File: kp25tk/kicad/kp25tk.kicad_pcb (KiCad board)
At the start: 2 copper layers, 97.5 x 159 mm, 60 parts, among them J1 Host Connector, J2 Config Header, J3 Power In, J4 Row Select In, J5 Column Out, J6 NMI Out, J7 Reset Out, J8 Switch, SW0 KEY00, SW1 KEY01, SW10 KEY0A, SW11 KEY0B, SW12 KEY0C, SW13 KEY0D, SW14 KEY0E, SW15 KEY0F, SW16 KEY10, SW17 KEY11, SW18 KEY12, SW19 KEY13, SW2 KEY02, SW20 KEY14, SW21 KEY15, SW22 KEY16, SW23 KEY17, SW24 NMI, SW25 RESET, SW27 SWITCH, SW3 KEY03, SW4 KEY04, SW5 KEY05, SW6 KEY06, SW7 KEY07, SW8 KEY08, SW9 KEY09, U1 74LS14

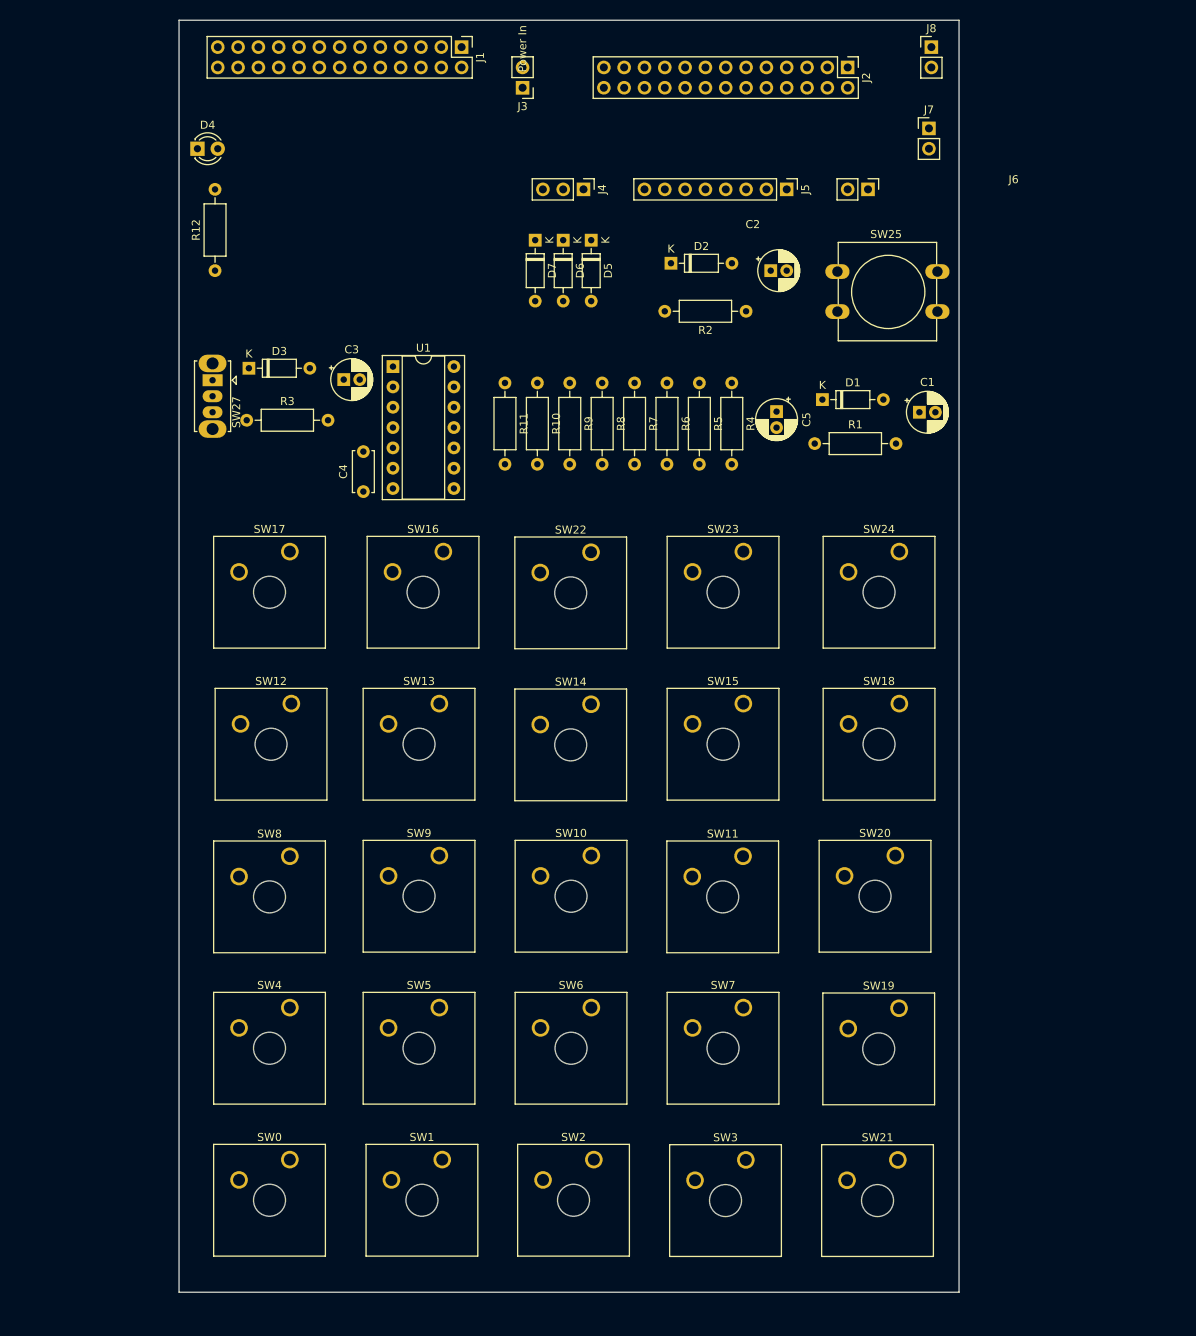
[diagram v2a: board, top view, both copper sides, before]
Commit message: kp25tk/: v0.0.4 Use resistor array and greatly compactify top of PCB
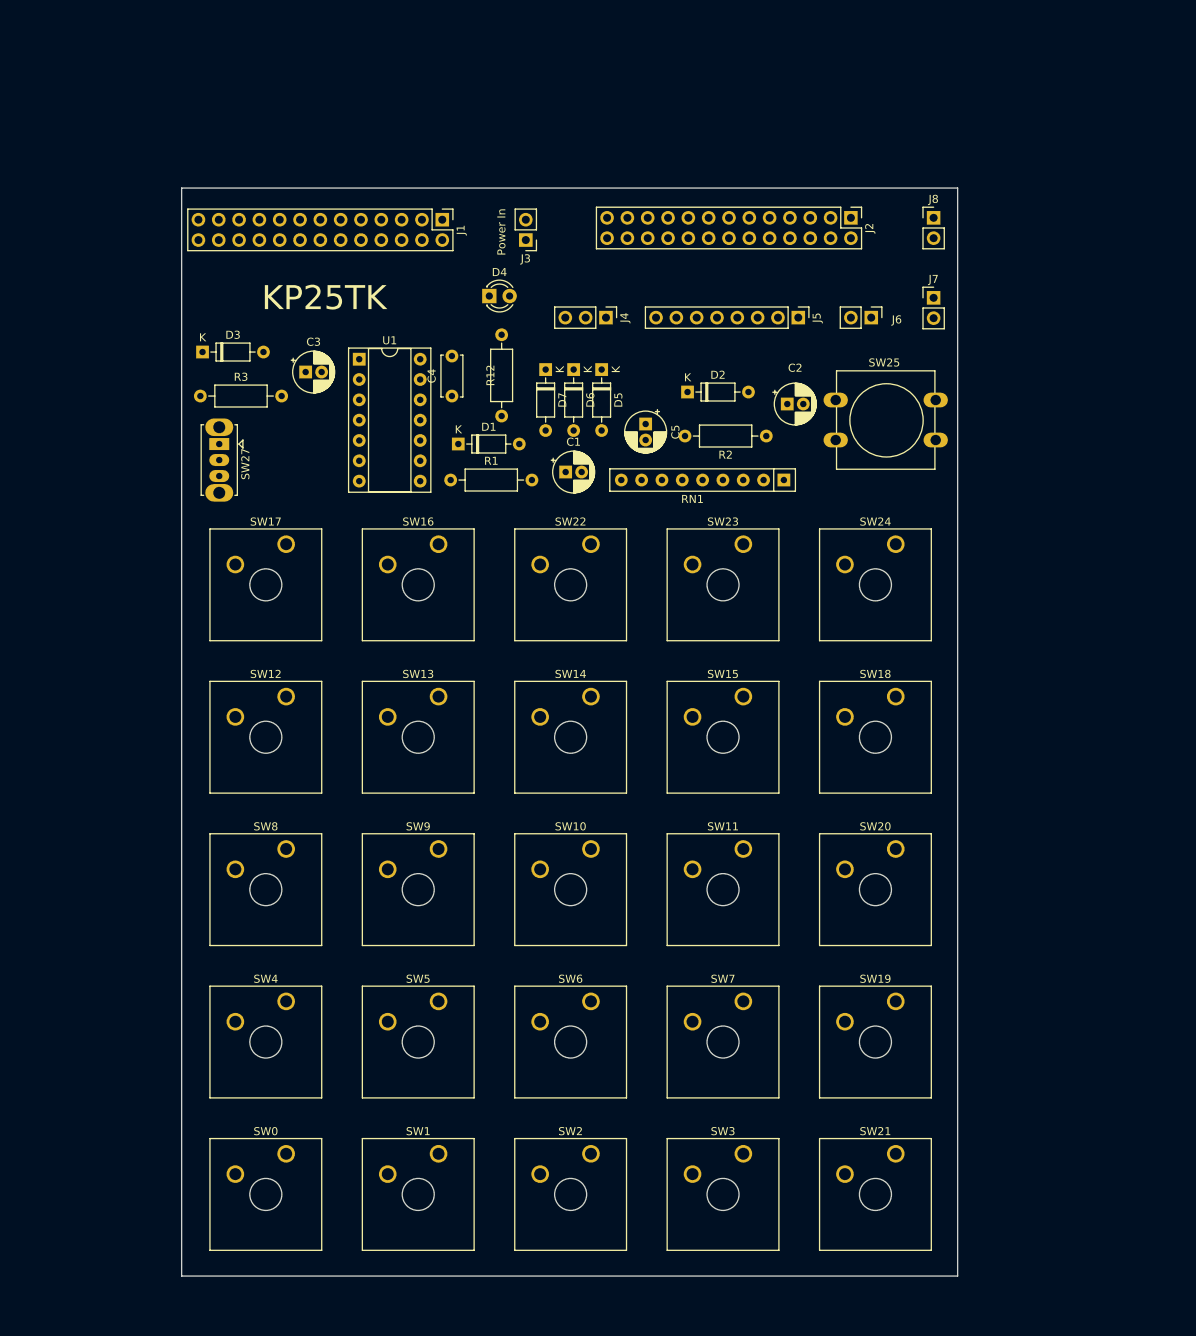
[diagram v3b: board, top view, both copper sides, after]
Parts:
- removed R10, R11, R4, R5, R6, R7, R8, R9: 33K, Resistor_THT:R_Axial_DIN0207_L6.3mm_D2.5mm_P10.16mm_Horizontal
- added RN1: 22K, Resistor_THT:R_Array_SIP9, F.Cu at (121.6, 82.1)
- moved D1 45.8 mm to (80.9, 77.6)
- moved R1 45.7 mm to (79.9, 82.1)
- moved C1 44.8 mm to (94.3, 81.1)
- moved D4 40.9 mm to (84.7, 59.1)
- moved R12 40.2 mm to (86.3, 74.1)
- moved J1 21.7 mm to (78.9, 49.5)
- moved J8 21.3 mm to (140.3, 49.3)
- moved J7 21.2 mm to (140.3, 59.3)
- moved J3 19.0 mm to (89.3, 52.1)
- moved J2 18.8 mm to (129.9, 49.3)
- moved C2 16.8 mm to (122.0, 72.6)
- moved C5 16.4 mm to (104.3, 75.1)
- moved C4 16.3 mm to (80.1, 71.6)
- moved J4 16.3 mm to (99.3, 61.8)
- moved D2 16.2 mm to (109.5, 71.1)
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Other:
- board size 97.5 x 159 mm -> 97 x 136 mm

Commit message: kp25tk/: v0.0.5 Schottky diodes, diodes in matrix
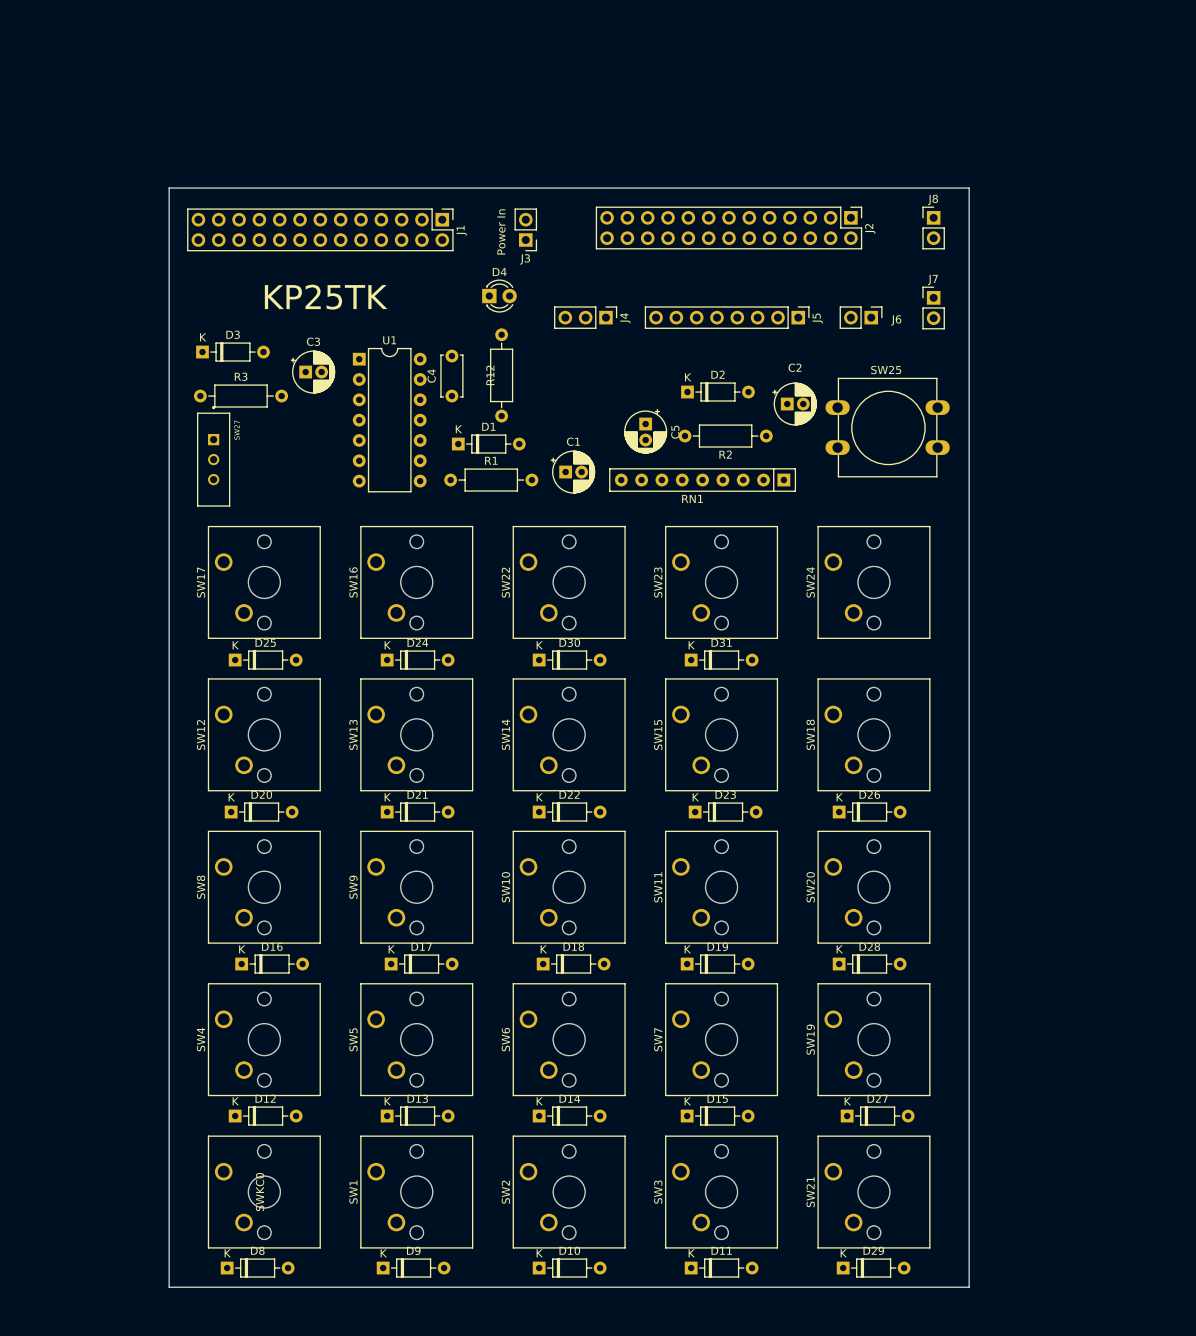
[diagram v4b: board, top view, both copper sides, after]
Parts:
- removed D5, D6, D7: 1N4148, Diode_THT:D_DO-35_SOD27_P7.62mm_Horizontal
- added D10: 1N5819, Diode_THT:D_DO-35_SOD27_P7.62mm_Horizontal, F.Cu at (91.0, 180.6)
- added D11: 1N5819, Diode_THT:D_DO-35_SOD27_P7.62mm_Horizontal, F.Cu at (110.0, 180.6)
- added D12: 1N5819, Diode_THT:D_DO-35_SOD27_P7.62mm_Horizontal, F.Cu at (53.0, 161.6)
- added D13: 1N5819, Diode_THT:D_DO-35_SOD27_P7.62mm_Horizontal, F.Cu at (72.0, 161.6)
- added D14: 1N5819, Diode_THT:D_DO-35_SOD27_P7.62mm_Horizontal, F.Cu at (91.0, 161.6)
- added D15: 1N5819, Diode_THT:D_DO-35_SOD27_P7.62mm_Horizontal, F.Cu at (109.5, 161.6)
- added D16: 1N5819, Diode_THT:D_DO-35_SOD27_P7.62mm_Horizontal, F.Cu at (53.8, 142.6)
- added D17: 1N5819, Diode_THT:D_DO-35_SOD27_P7.62mm_Horizontal, F.Cu at (72.5, 142.6)
- added D18: 1N5819, Diode_THT:D_DO-35_SOD27_P7.62mm_Horizontal, F.Cu at (91.5, 142.6)
- added D19: 1N5819, Diode_THT:D_DO-35_SOD27_P7.62mm_Horizontal, F.Cu at (109.5, 142.6)
- added D20: 1N5819, Diode_THT:D_DO-35_SOD27_P7.62mm_Horizontal, F.Cu at (52.5, 123.6)
- added D21: 1N5819, Diode_THT:D_DO-35_SOD27_P7.62mm_Horizontal, F.Cu at (72.0, 123.6)
- added D22: 1N5819, Diode_THT:D_DO-35_SOD27_P7.62mm_Horizontal, F.Cu at (91.0, 123.6)
- added D23: 1N5819, Diode_THT:D_DO-35_SOD27_P7.62mm_Horizontal, F.Cu at (110.5, 123.6)
- added D24: 1N5819, Diode_THT:D_DO-35_SOD27_P7.62mm_Horizontal, F.Cu at (72.0, 104.6)
- added D25: 1N5819, Diode_THT:D_DO-35_SOD27_P7.62mm_Horizontal, F.Cu at (53.0, 104.6)
- added D26: 1N5819, Diode_THT:D_DO-35_SOD27_P7.62mm_Horizontal, F.Cu at (128.5, 123.6)
- added D27: 1N5819, Diode_THT:D_DO-35_SOD27_P7.62mm_Horizontal, F.Cu at (129.5, 161.6)
- added D28: 1N5819, Diode_THT:D_DO-35_SOD27_P7.62mm_Horizontal, F.Cu at (128.5, 142.6)
- added D29: 1N5819, Diode_THT:D_DO-35_SOD27_P7.62mm_Horizontal, F.Cu at (129.0, 180.6)
- added D30: 1N5819, Diode_THT:D_DO-35_SOD27_P7.62mm_Horizontal, F.Cu at (91.0, 104.6)
- added D31: 1N5819, Diode_THT:D_DO-35_SOD27_P7.62mm_Horizontal, F.Cu at (110.0, 104.6)
- added D8: 1N5819, Diode_THT:D_DO-35_SOD27_P7.62mm_Horizontal, F.Cu at (52.0, 180.6)
- added D9: 1N5819, Diode_THT:D_DO-35_SOD27_P7.62mm_Horizontal, F.Cu at (71.5, 180.6)
- added SWKC0: Keycap, Button_Switch_Keyboard_Keycap:SW_Cherry_MX_Keycap_1.00u, F.Cu at (56.6, 171.1)
- added SWKC1: Keycap, Button_Switch_Keyboard_Keycap:SW_Cherry_MX_Keycap_1.00u, F.Cu at (75.7, 171.1)
- added SWKC10: Keycap, Button_Switch_Keyboard_Keycap:SW_Cherry_MX_Keycap_1.00u, F.Cu at (94.7, 133.0)
- added SWKC11: Keycap, Button_Switch_Keyboard_Keycap:SW_Cherry_MX_Keycap_1.00u, F.Cu at (113.8, 133.0)
- added SWKC12: Keycap, Button_Switch_Keyboard_Keycap:SW_Cherry_MX_Keycap_1.00u, F.Cu at (56.6, 113.9)
- added SWKC13: Keycap, Button_Switch_Keyboard_Keycap:SW_Cherry_MX_Keycap_1.00u, F.Cu at (75.7, 113.9)
- added SWKC14: Keycap, Button_Switch_Keyboard_Keycap:SW_Cherry_MX_Keycap_1.00u, F.Cu at (94.7, 113.9)
- added SWKC15: Keycap, Button_Switch_Keyboard_Keycap:SW_Cherry_MX_Keycap_1.00u, F.Cu at (113.8, 113.9)
- added SWKC16: Keycap, Button_Switch_Keyboard_Keycap:SW_Cherry_MX_Keycap_1.00u, F.Cu at (75.7, 94.9)
- added SWKC17: Keycap, Button_Switch_Keyboard_Keycap:SW_Cherry_MX_Keycap_1.00u, F.Cu at (56.6, 94.9)
- added SWKC18: Keycap, Button_Switch_Keyboard_Keycap:SW_Cherry_MX_Keycap_1.00u, F.Cu at (132.8, 113.9)
- added SWKC19: Keycap, Button_Switch_Keyboard_Keycap:SW_Cherry_MX_Keycap_1.00u, F.Cu at (132.8, 152.0)
- added SWKC2: Keycap, Button_Switch_Keyboard_Keycap:SW_Cherry_MX_Keycap_1.00u, F.Cu at (94.7, 171.1)
- added SWKC20: Keycap, Button_Switch_Keyboard_Keycap:SW_Cherry_MX_Keycap_1.00u, F.Cu at (132.8, 133.0)
- added SWKC21: Keycap, Button_Switch_Keyboard_Keycap:SW_Cherry_MX_Keycap_1.00u, F.Cu at (132.8, 171.1)
- added SWKC22: Keycap, Button_Switch_Keyboard_Keycap:SW_Cherry_MX_Keycap_1.00u, F.Cu at (94.7, 94.9)
- added SWKC23: Keycap, Button_Switch_Keyboard_Keycap:SW_Cherry_MX_Keycap_1.00u, F.Cu at (113.8, 94.9)
- added SWKC24: Keycap, Button_Switch_Keyboard_Keycap:SW_Cherry_MX_Keycap_1.00u, F.Cu at (132.8, 94.9)
- added SWKC3: Keycap, Button_Switch_Keyboard_Keycap:SW_Cherry_MX_Keycap_1.00u, F.Cu at (113.8, 171.1)
- added SWKC4: Keycap, Button_Switch_Keyboard_Keycap:SW_Cherry_MX_Keycap_1.00u, F.Cu at (56.6, 152.0)
- added SWKC5: Keycap, Button_Switch_Keyboard_Keycap:SW_Cherry_MX_Keycap_1.00u, F.Cu at (75.7, 152.0)
- added SWKC6: Keycap, Button_Switch_Keyboard_Keycap:SW_Cherry_MX_Keycap_1.00u, F.Cu at (94.7, 152.0)
- added SWKC7: Keycap, Button_Switch_Keyboard_Keycap:SW_Cherry_MX_Keycap_1.00u, F.Cu at (113.8, 152.0)
- added SWKC8: Keycap, Button_Switch_Keyboard_Keycap:SW_Cherry_MX_Keycap_1.00u, F.Cu at (56.6, 133.0)
- added SWKC9: Keycap, Button_Switch_Keyboard_Keycap:SW_Cherry_MX_Keycap_1.00u, F.Cu at (75.7, 133.0)
- D1, D2, D3: value 1N4148 -> 1N5819
- SW0, SW1, SW10, SW11, SW12, SW13, SW14, SW15, SW16, SW17, SW18, SW19, SW2, SW20, SW21, SW22, SW23, SW24, SW3, SW4, SW5, SW6, SW7, SW8, SW9: footprint Button_Switch_Keyboard:SW_Cherry_MX_1.00u_Plate -> Button_Switch_Keyboard:SW_Cherry_MX_1.00u_PCB
- SW27: footprint Button_Switch_THT:SW_Slide_1P2T_CK_OS102011MS2Q -> Button_Switch_THT_Extras:SW_MINI-SPDT-SW
- U1: footprint Package_DIP:DIP-14_W7.62mm_Socket -> Package_DIP:DIP-14_W7.62mm
- moved SW19 8.12 mm to (127.7, 149.5), turned to 90 degrees
- moved SW5 8.12 mm to (70.6, 149.5), turned to 90 degrees
- moved SW6 8.12 mm to (89.6, 149.5), turned to 90 degrees
- moved SW7 8.12 mm to (108.7, 149.5), turned to 90 degrees
- moved SW13 8.12 mm to (70.6, 111.4), turned to 90 degrees
- moved SW14 8.12 mm to (89.6, 111.4), turned to 90 degrees
- moved SW15 8.12 mm to (108.7, 111.4), turned to 90 degrees
- moved SW16 8.12 mm to (70.6, 92.3), turned to 90 degrees
- moved SW18 8.12 mm to (127.7, 111.4), turned to 90 degrees
- moved SW22 8.12 mm to (89.6, 92.3), turned to 90 degrees
- moved SW23 8.12 mm to (108.7, 92.3), turned to 90 degrees
- moved SW24 8.12 mm to (127.7, 92.3), turned to 90 degrees
- moved SW4 8.12 mm to (51.5, 149.5), turned to 90 degrees
- moved SW1 8.12 mm to (70.6, 168.5), turned to 90 degrees
- moved SW10 8.12 mm to (89.6, 130.4), turned to 90 degrees
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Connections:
- SW0 pad 2: Net-(D5-A) -> Net-(D8-A)
- SW1 pad 2: Net-(D5-A) -> Net-(D9-A)
- SW10 pad 2: Net-(D6-A) -> Net-(D18-A)
- SW11 pad 2: Net-(D6-A) -> Net-(D19-A)
- SW12 pad 2: Net-(D6-A) -> Net-(D20-A)
- SW13 pad 2: Net-(D6-A) -> Net-(D21-A)
- SW14 pad 2: Net-(D6-A) -> Net-(D22-A)
- SW15 pad 2: Net-(D6-A) -> Net-(D23-A)
- SW16 pad 2: Net-(D7-A) -> Net-(D24-A)
- SW17 pad 2: Net-(D7-A) -> Net-(D25-A)
- SW18 pad 2: Net-(D7-A) -> Net-(D26-A)
- SW19 pad 2: Net-(D7-A) -> Net-(D27-A)
- SW2 pad 2: Net-(D5-A) -> Net-(D10-A)
- SW20 pad 2: Net-(D7-A) -> Net-(D28-A)
- SW21 pad 2: Net-(D7-A) -> Net-(D29-A)
- SW22 pad 2: Net-(D7-A) -> Net-(D30-A)
- SW23 pad 2: Net-(D7-A) -> Net-(D31-A)
- SW3 pad 2: Net-(D5-A) -> Net-(D11-A)
- SW4 pad 2: Net-(D5-A) -> Net-(D12-A)
- SW5 pad 2: Net-(D5-A) -> Net-(D13-A)
- SW6 pad 2: Net-(D5-A) -> Net-(D14-A)
- SW7 pad 2: Net-(D5-A) -> Net-(D15-A)
- SW8 pad 2: Net-(D6-A) -> Net-(D16-A)
- SW9 pad 2: Net-(D6-A) -> Net-(D17-A)
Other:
- board size 97 x 136 mm -> 100 x 137.4 mm

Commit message: kp25tk/: v0.0.6 SPDT switch, improve PCB component locations/labels
We still need to go through and fix all the keyswitch labels to be
just the key name, without the SWnn.
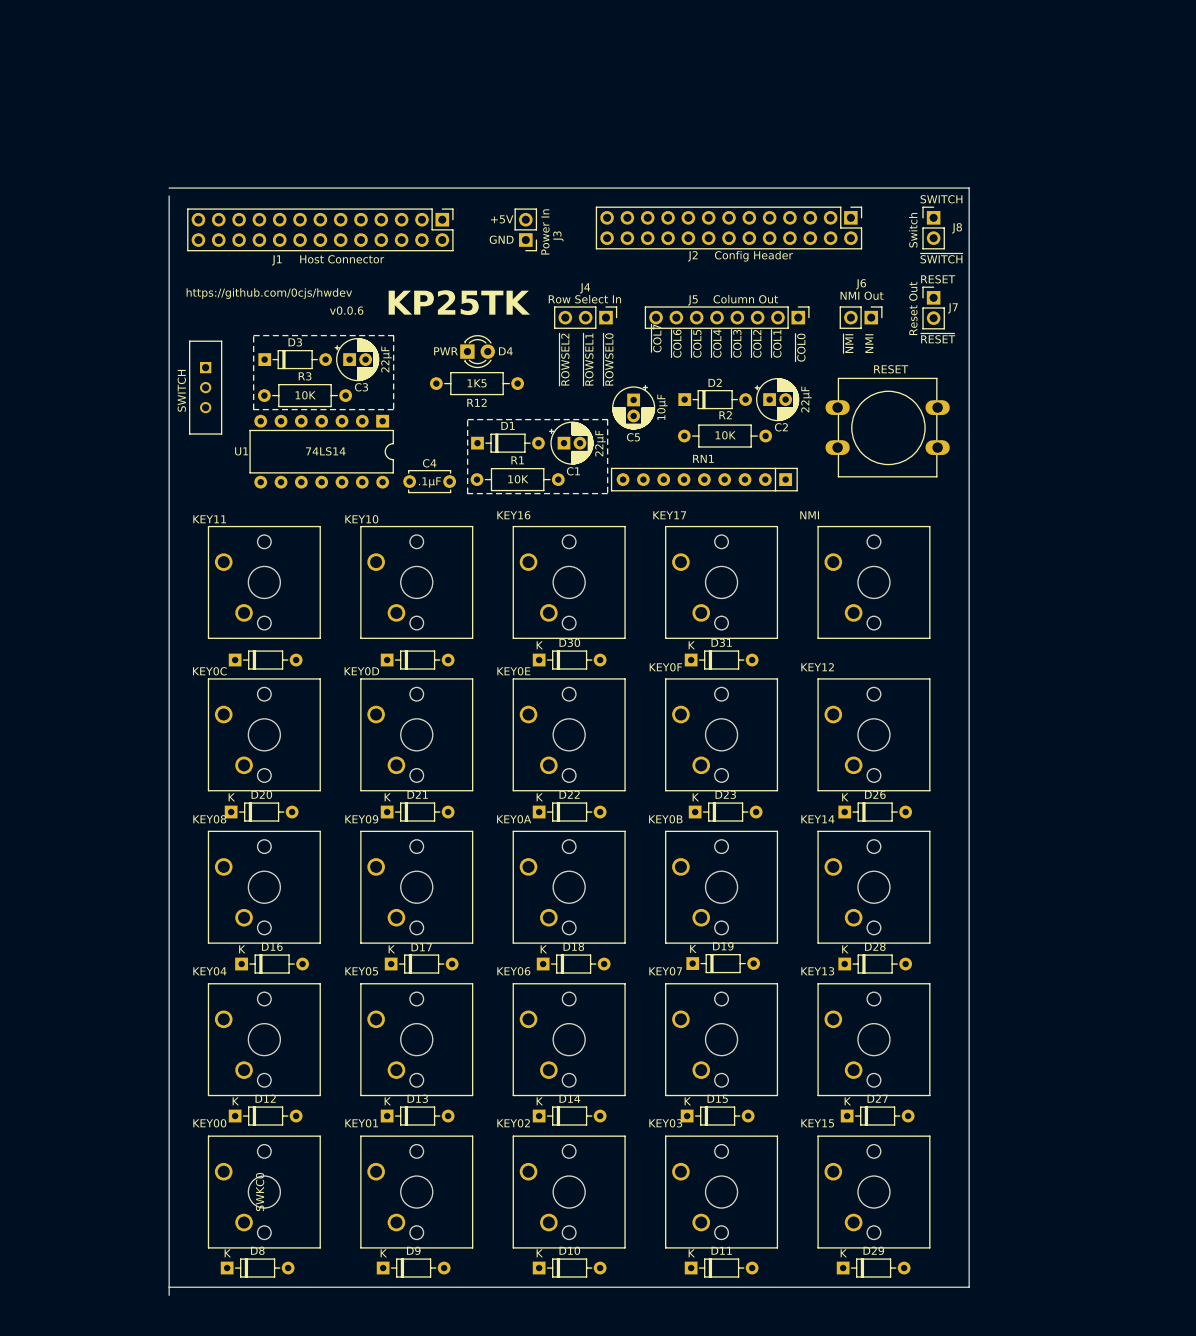
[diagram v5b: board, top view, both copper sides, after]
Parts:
- C4: value 0.1µF -> .1µF
- moved C4 10.7 mm to (79.8, 82.2), turned to 180 degrees
- moved SW27 9.06 mm to (49.3, 70.5)
- moved U1 8.28 mm to (71.4, 74.7), turned to -90 degrees
- moved R3 8.00 mm to (56.6, 71.5)
- moved D3 7.83 mm to (56.7, 67.0)
- moved D4 7.46 mm to (82.0, 66.0)
- moved C3 5.72 mm to (67.3, 67.0)
- moved R12 4.52 mm to (88.3, 70.0), turned to 180 degrees
- moved C1 3.62 mm to (94.1, 77.4)
- moved C5 3.36 mm to (102.8, 72.0)
- moved R1 3.30 mm to (83.2, 82.0)
- moved D1 2.40 mm to (83.3, 77.4)
- moved C2 2.27 mm to (119.8, 72.0)
- moved D2 1.01 mm to (109.2, 72.0)
- moved D19 0.69 mm to (110.2, 142.5)
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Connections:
- SW27 pad 1: Net-(D3-A) -> Earth
- SW27 pad 2: Earth -> Net-(D3-A)
- SW27 pad 3: (no net) -> unconnected-(SW27-C-Pad3)
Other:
- board size 100 x 137.4 mm -> 100 x 138.4 mm
- board text added: "https://github.com/0cjs/hwdev"
- board text added: "v${REVISION}"
